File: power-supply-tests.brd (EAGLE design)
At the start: 20 x 20 mm, 16 parts, among them U2 POWER-VREG-EN-SW-500MA

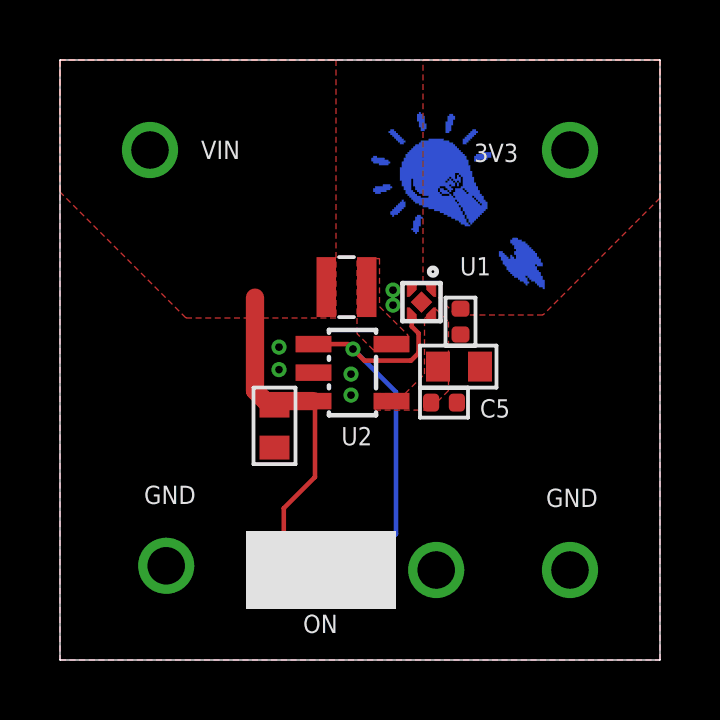
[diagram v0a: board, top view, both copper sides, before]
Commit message: Latest changes to nRF91
Changed:
* Power supply inductor
* Power supply tests board updated
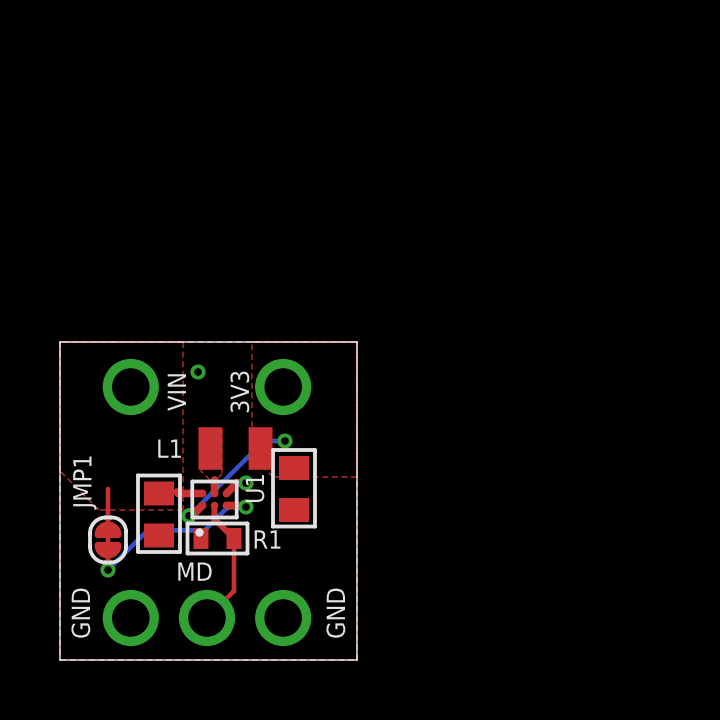
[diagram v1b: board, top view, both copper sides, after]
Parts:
- removed C2: 10u, wolff-den:C0603
- removed C3: 1u, wolff-den:CAPC1005X55N
- removed TP2, TP6, TP7: HEADER-1, wolff-den:CON-HEADER-1X1-POGO-1P9
- removed U$1: (no value), wolff-den:LOGO-CIRCUITDOJO-BULB
- removed U$2: (no value), wolff-den:LOGO-CIRCUITDOJO
- removed U2: POWER-VREG-EN-SW-500MA, wolff-den:SOT25
- added JMP1: JUMPER-NC, wolff-den:JUMPER-ROUND-NC
- added R1: 1M, wolff-den:R0402-M
- added TP8: HEADER-1, wolff-den:CON-HEADER-1X1-POGO-1P9
- C1: value 10u -> 2.2u
- C5: value 1u -> 2.2u; device wolff-den:CAPC1005X55N -> wolff-den:C0603
- L1: value 4.7u -> 470nH; device wolff-den:IND-2P0X2P0X1P2 -> wolff-den:INDC2012X100N
- U1: value (none) -> IC-LM3281YFQR; device wolff-den:DFN4 -> wolff-den:BGA6N40P2X3_116X143X67N
- moved TP3 12.4 mm to (7.44, 9.10)
- moved C5 10.2 mm to (3.30, 4.85), turned to 270 degrees
- moved TP5 9.69 mm to (7.44, 1.40)
- moved U1 9.53 mm to (5.15, 5.35), turned to 90 degrees
- moved TP1 7.93 mm to (2.36, 9.10)
- moved C1 6.85 mm to (7.80, 5.70), turned to 270 degrees
- moved L1 6.53 mm to (5.85, 7.05)
- moved TP4 2.10 mm to (2.36, 1.40)
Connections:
- removed net N$1: L1.P$2, U2.5
- removed net N$3: C1.1, C5.1, U1.4, U2.4
- new net PS_MODE: R1.2, TP8.1, U1.B1
- new net PS_SW1: L1.1, U1.B2
- net +3V3: now also C1.1, L1.2, U1.A1; no longer C3.1, U1.1
- net GND: now also R1.1, U1.C2; no longer C2.2, C3.2, TP7.1, U1.2, U2.2
- net PS_EN: now also JMP1.P$1, U1.C1; no longer TP2.1, U1.3, U2.1
- net VSYS: now also C5.1, JMP1.P$2, U1.A2; no longer C2.1, L1.P$1, TP6.1, U2.3
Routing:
- net VSYS: track 11.8 -> 2.27 mm
- net PS_EN: track 13.6 -> 6.84 mm, vias 1 -> 2
- net +3V3: track 0.00 -> 4.83 mm, vias 0 -> 2
- net PS_MODE: track 0.00 -> 4.39 mm
- net GND: track 0.00 -> 0.59 mm, vias 6 -> 2
- added copper zone on layer 1, net PS_SW1
- removed copper zone on layer 1, net N$1
- removed copper zone on layer 1, net N$3
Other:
- board size 20 x 20 mm -> 9.9 x 10.6 mm
- board text added: "MD"
- board text removed: "ON"
